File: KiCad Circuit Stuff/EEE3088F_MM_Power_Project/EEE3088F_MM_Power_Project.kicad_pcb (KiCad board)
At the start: 2 copper layers, 85 parts, among them J1 Conn_01x02, J2 Conn_02x16_Odd_Even, U1 MT3608, U10 DRV8833PWP, U11 SS-12D06-G050, U12 AP22814AW5-7, U14 AP22814AW5-7, U2 INA219AIDCNR, U3 AMS1117-3.3, U4 TPS5430DDAR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

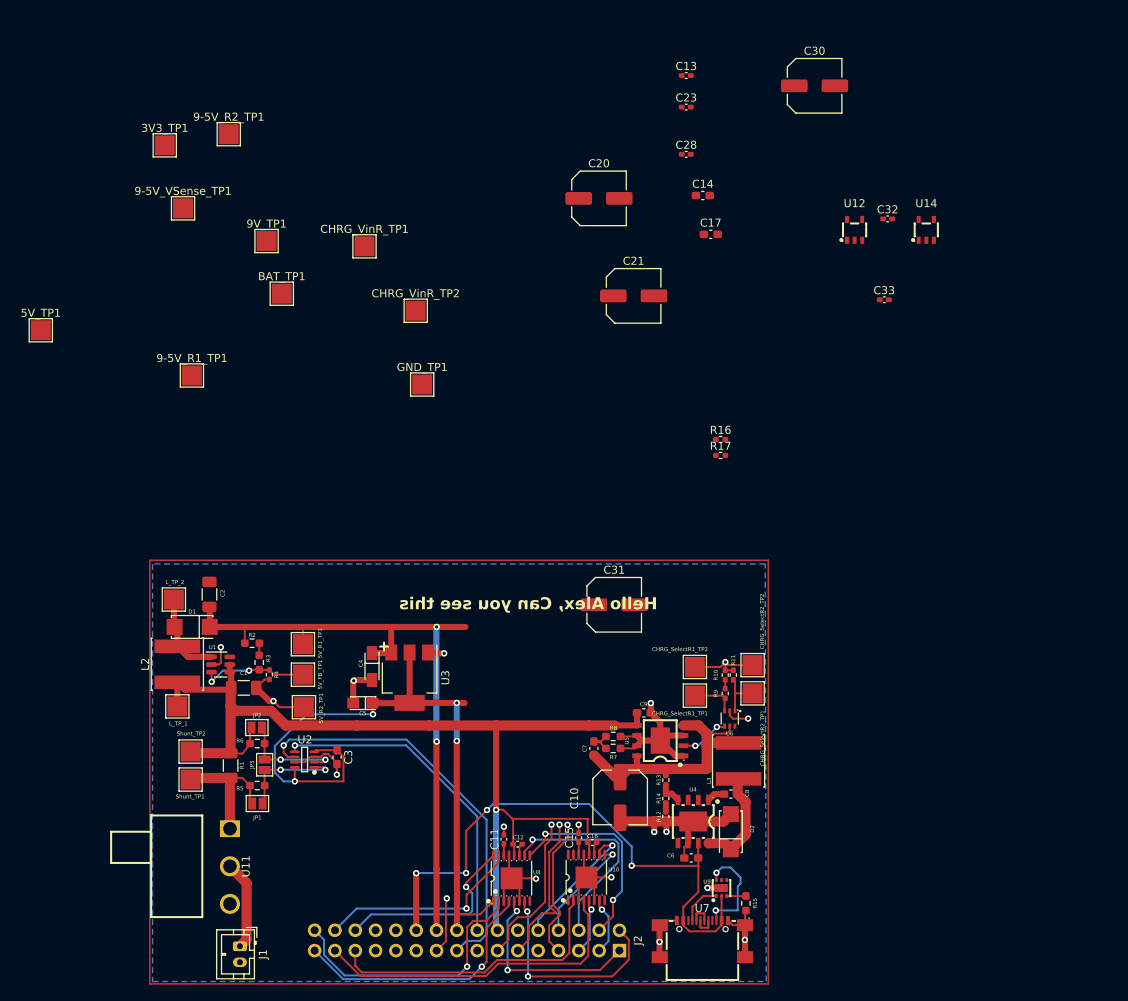
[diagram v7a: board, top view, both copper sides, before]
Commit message: Added most of all connections and holes
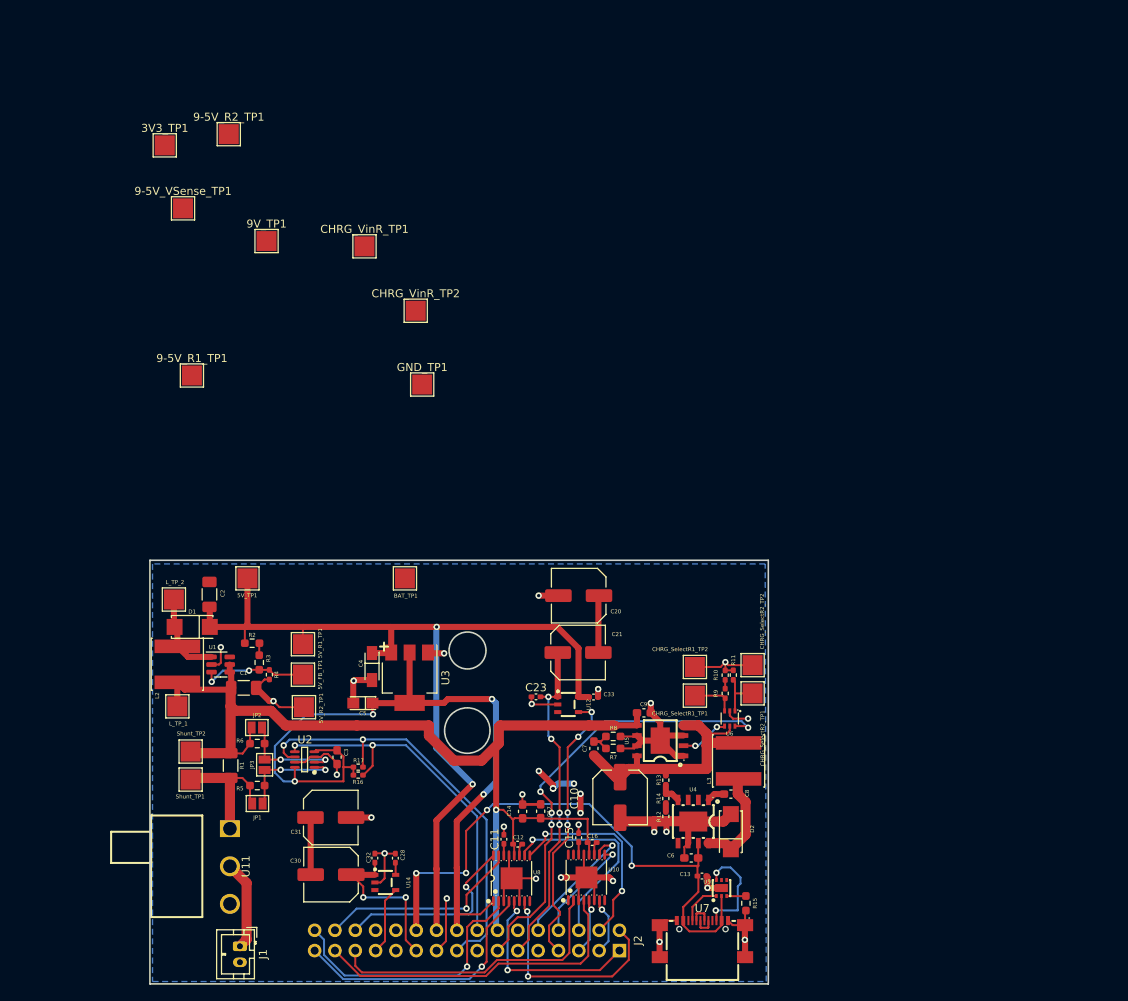
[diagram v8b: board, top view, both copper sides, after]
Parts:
- moved C30 115.7 mm to (122.6, 139.3), turned to 180 degrees
- moved U14 106.0 mm to (129.4, 140.3), turned to -90 degrees
- moved C32 102.4 mm to (128.1, 137.2), turned to -90 degrees
- moved C13 100.1 mm to (169.0, 139.5), turned to 180 degrees
- moved C28 95.2 mm to (130.7, 137.2), turned to -90 degrees
- moved C14 80.2 mm to (146.6, 131.4), turned to 90 degrees
- moved C23 76.1 mm to (148.3, 117.1)
- moved C17 75.2 mm to (148.8, 131.4), turned to 90 degrees
- moved U12 69.3 mm to (152.3, 118.0), turned to -90 degrees
- moved R16 61.7 mm to (126.0, 126.9), turned to 180 degrees
- moved C33 61.5 mm to (155.4, 117.1), turned to 180 degrees
- moved R17 59.8 mm to (126.0, 125.9), turned to 180 degrees
- moved C20 56.8 mm to (153.5, 111.5)
- moved C31 44.3 mm to (122.6, 132.2)
- moved 5V_TP1 40.4 mm to (112.2, 102.3)
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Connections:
- BAT_TP1 pad 1: /Battery -> /Battery_Out
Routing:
- net /Fast_Charge_CTRL: track 19.4 -> 56.2 mm, vias 1 -> 4
- net GND: track 133.1 -> 169.5 mm, vias 18 -> 31
- net +5V: track 82.4 -> 116.5 mm
- net /EXT_LOAD2_OUT: track 19.7 -> 42.2 mm, vias 1 -> 4
- net /EXT_LOAD1_OUT: track 0.00 -> 20.5 mm, vias 0 -> 2
- net /CTRL_EXT_LOAD2: track 17.9 -> 34.9 mm, vias 1 -> 4
- net /CTRL_EXT_LOAD1: track 0.00 -> 8.60 mm
- net +3V3: track 88.1 -> 96.7 mm
- net Net-(C30-Pad2): track 0.00 -> 7.15 mm
- net Net-(C20-Pad2): track 0.00 -> 7.14 mm
- net /I2C1_SCL: track 41.5 -> 45.8 mm, vias 1 -> 2
- net /I2C1_SDA: track 51.2 -> 54.7 mm, vias 1 -> 2
- net /Battery_Out: track 132.3 -> 135.7 mm
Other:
- board outline added: 77.3 x 52.9 mm
- board text removed: "Hello Alex, Can you see this"
